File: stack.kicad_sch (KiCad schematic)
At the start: 111 parts, among them CN1 10nF, CN2 10nF, CN3 10nF, CN4 10nF, CN5 10nF, CN6 10nF, CN7 10nF, J5 CELLS, J6 TEMP0, J7 TEMP1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

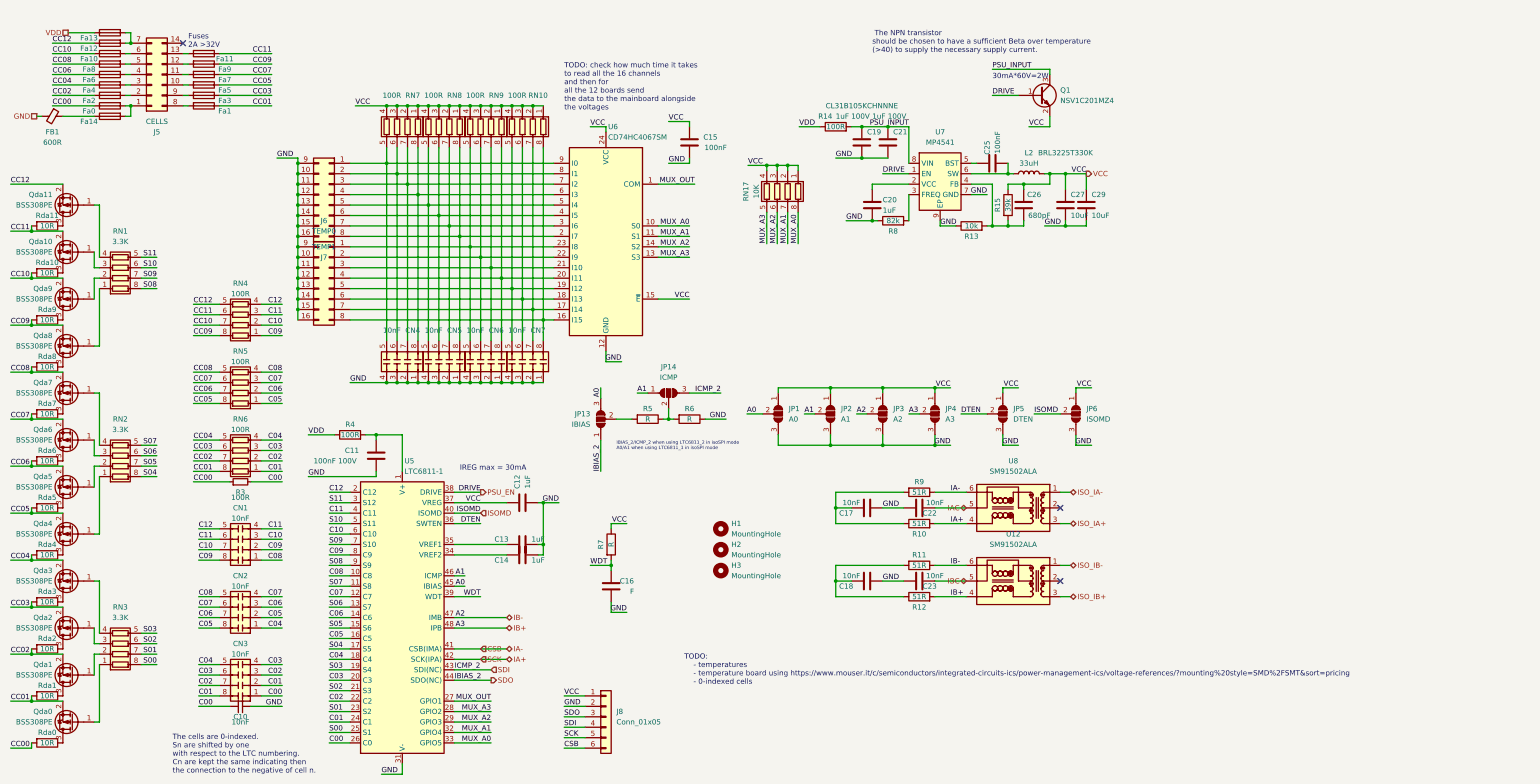
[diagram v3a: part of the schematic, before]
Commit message: fix
- Changed oscillator footprint
- tied mux enable to ground
- Corrected power BJT's footprint
- added 5V presence led
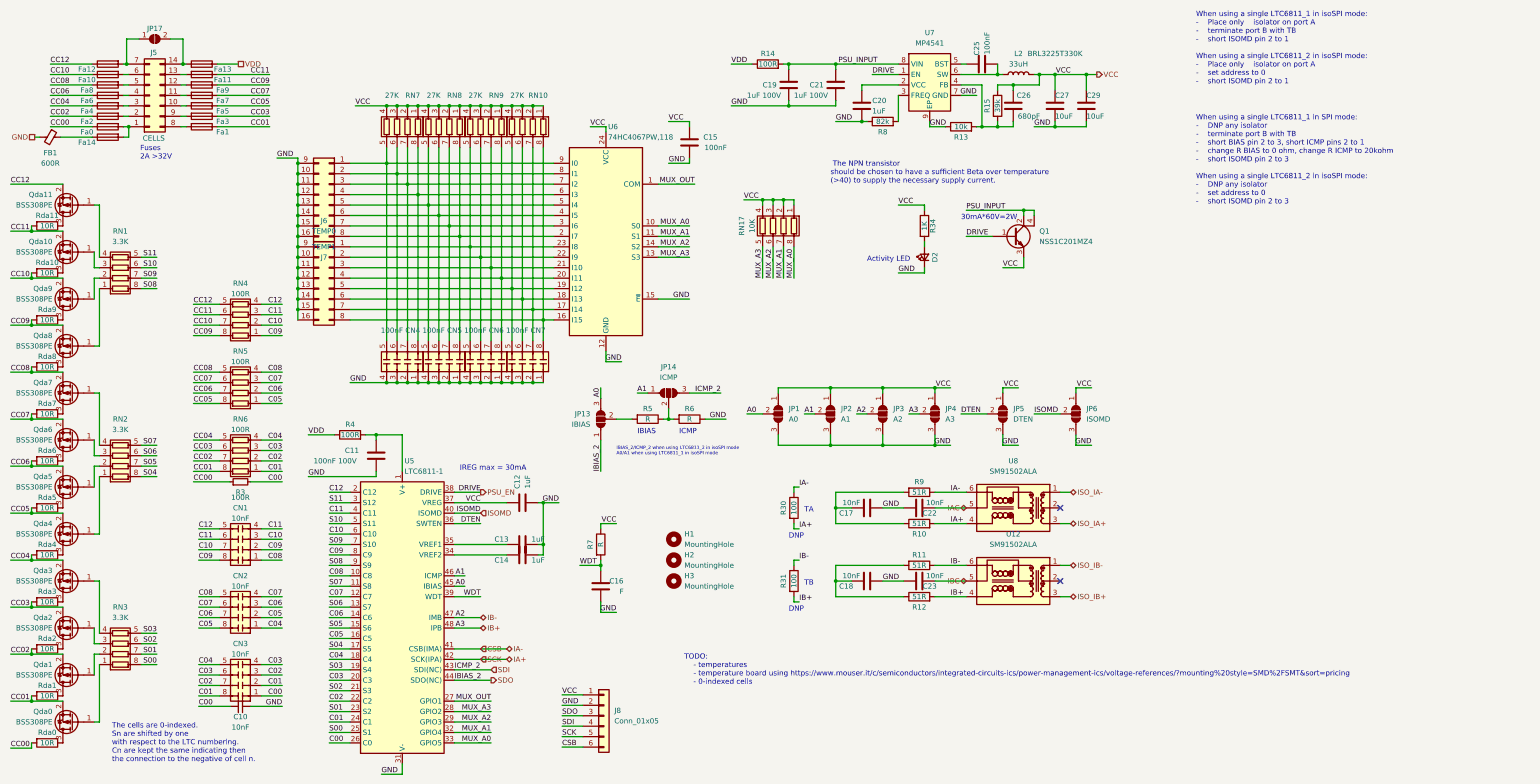
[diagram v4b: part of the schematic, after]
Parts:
- removed Q1: NSV1C201MZ4, Package_TO_SOT_SMD:SOT-223-3_TabPin2, symbol Device:Q_NPN_BEC
- added D2: LED_Small, LED_SMD:LED_0603_1608Metric, symbol Device:LED_Small
- added JP17: isoIP, Jumper:SolderJumper-2_P1.3mm_Open_RoundedPad1.0x1.5mm, symbol Jumper:SolderJumper_2_Open
- added Q1: NSS1C201MZ4, Package_TO_SOT_SMD:SOT-223, symbol Device:Q_NPN_BCEC
- added R30, R31: 100, Resistor_SMD:R_0603_1608Metric, symbol Device:R
- added R34: 1K, Resistor_SMD:R_0603_1608Metric, symbol Device:R
- CN4, CN5, CN6, CN7: value 10nF -> 100nF
- RN10, RN7, RN8, RN9: value 100R -> 27K
- U6: value CD74HC4067SM -> 74HC4067PW,118; footprint Package_SO:SSOP-24_5.3x8.2mm_P0.65mm -> Package_SO:TSSOP-24_4.4x7.8mm_P0.65mm
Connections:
- net CSB: now also R30.1
- net GND: now also U6.15 (~{E}), D2.1 (K)
- net IA+: now also R30.2
- net IB+: now also R31.2
- net IB-: now also R31.1
- net PSU_EN: now also Q1.1 (B)
- net PSU_INPUT: now also Q1.2 (C), Q1.4 (C)
- net VCC: now also Q1.3 (E), R34.1; no longer U6.15 (~{E})
- net at Fa12.2, J5.7 (Pin_7): now also JP17.1 (A); no longer Fa13.2
- net at J5.14 (Pin_14): now also Fa13.2, JP17.2 (B)
- new net: D2.2 (A), R34.2
- no-connect marks 3 -> 2
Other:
- note added: "Activity LED"
- note added: "DNP"
- note added: "IBIAS"
- note added: "ICMP"
- note added: "TA"
- note added: "TB"
- note added: "When using a single LTC6811_1 in SPI mode: - DNP any isolator - terminate port B with TB - short BIAS pin 2 to 3, short ICMP pins 2 to 1 - change R BIAS to 0 ohm, change R ICMP to 20kohm - short ISOMD pin 2 to 3 When using a single LTC6811_2 in isoSPI mode: - DNP any isolator - set address to 0 - short ISOMD pin 2 to 3"
- note added: "When using a single LTC6811_1 in isoSPI mode: - Place only isolator on port A - terminate port B with TB - short ISOMD pin 2 to 1 When using a single LTC6811_2 in isoSPI mode: - Place only isolator on port A - set address to 0 - short ISOMD pin 2 to 1"
- note removed: "TODO: check how much time it takes to read all the 16 channels and then for all the 12 boards send the data to the mainboard alongside the voltages"
- moved on the sheet: C16, C19, C20, C21, C25, C26, C27, C29, FB1, Fa0, Fa1, Fa10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
